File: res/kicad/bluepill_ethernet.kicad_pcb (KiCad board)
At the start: 2 copper layers, 50.4 x 50.4 mm, 47 parts, among them J1 HEADER-1x20, J2 Conn_01x03, J3 Conn_02x05_Odd_Even, J4 HEADER-1x20, J5 Conn_02x02_Odd_Even, J7 Conn_02x04_Odd_Even, SW1 SW_Push, U1 BluePill_STM32F103C, U2 93C46, U3 WIZ850io, U4 93C46, U5 PCF8574A, U6 LM75B

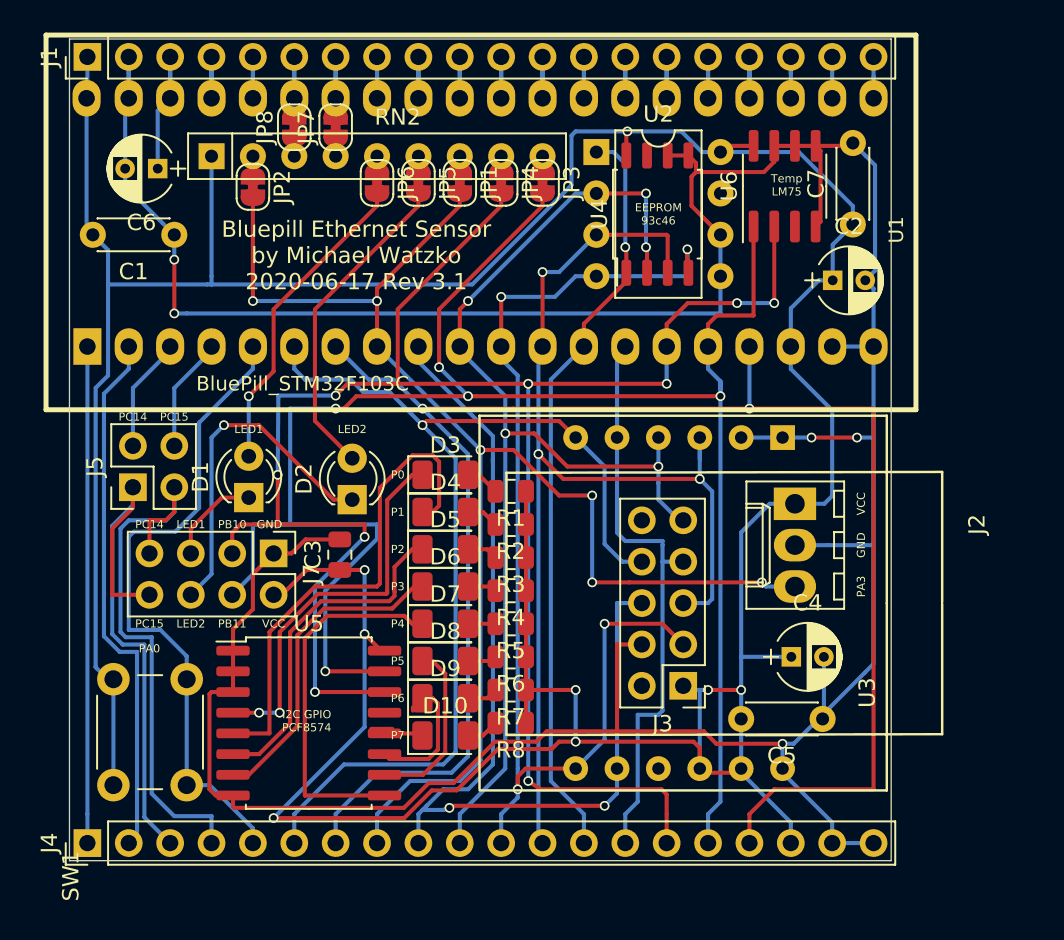
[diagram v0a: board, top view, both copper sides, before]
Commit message: Move molex pins and w5500 into 2,54mm raster
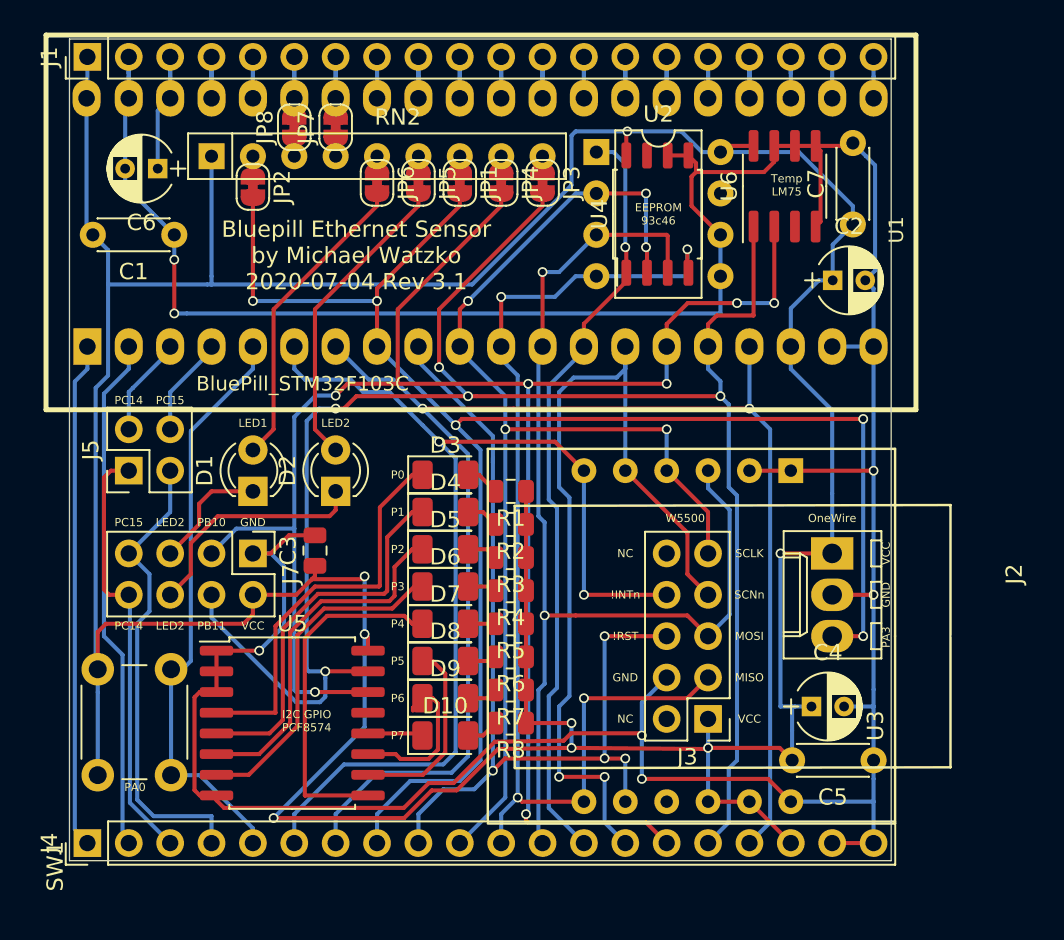
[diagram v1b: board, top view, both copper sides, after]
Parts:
- moved C5 4.03 mm to (92.2, 74.9)
- moved J2 3.81 mm to (89.7, 62.2)
- moved C4 3.29 mm to (88.4, 71.6)
- moved J3 2.54 mm to (82.0, 72.4)
- moved U3 2.09 mm to (87.1, 67.3)
- moved C3 1.55 mm to (57.9, 62.1)
- moved J7 1.27 mm to (54.1, 62.2)
- moved SW1 1.14 mm to (44.6, 75.8)
- moved D2 1.14 mm to (59.2, 58.4)
- moved J5 1.05 mm to (46.5, 57.1)
- moved U5 1.01 mm to (56.5, 72.6)
- moved D1 0.46 mm to (54.1, 58.4)
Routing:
- net Net-(J3-Pad7): track 36.1 -> 55.6 mm, vias 0 -> 2
- net Net-(J2-Pad3): track 88.9 -> 103.4 mm, vias 6 -> 5
- net Net-(J4-Pad17): track 105.7 -> 92.4 mm
- net VCC: track 248.8 -> 257.4 mm
- net Net-(J4-Pad3): track 34.0 -> 26.5 mm
- net Net-(D4-Pad1): track 30.8 -> 23.5 mm
- net i2c1c: track 123.7 -> 116.9 mm, vias 9 -> 7
- net Net-(D2-Pad1): track 21.0 -> 14.6 mm, vias 1 -> 0
- net Net-(J4-Pad4): track 34.4 -> 28.7 mm
- net Net-(J4-Pad5): track 40.2 -> 36.1 mm
- net Net-(J3-Pad6): track 61.3 -> 58.0 mm, vias 2 -> 4
- net i2c1d: track 118.2 -> 115.2 mm
- net Net-(J3-Pad9): track 70.3 -> 72.9 mm
- net Net-(J3-Pad8): track 64.8 -> 67.2 mm, vias 1 -> 2
- net Net-(J3-Pad5): track 69.9 -> 68.0 mm, vias 3 -> 2
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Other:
- board text added: "!INTn"
- board text added: "!RST"
- board text added: "Bluepill Ethernet Sensor by Michael Watzko 2020-07-04 Rev 3.1"
- board text added: "MISO"
- board text added: "MOSI"
- board text added: "NC"
- board text added: "OneWire"
- board text added: "SCLK"
- board text added: "SCNn"
- board text added: "W5500"
- board text removed: "Bluepill Ethernet Sensor by Michael Watzko 2020-06-17 Rev 3.1"

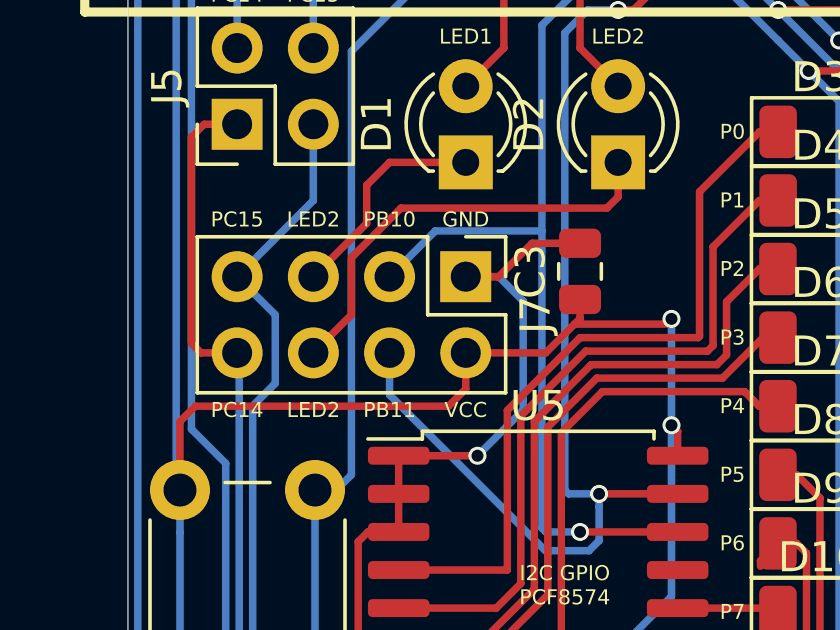
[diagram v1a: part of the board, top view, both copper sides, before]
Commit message: Add SCL and SDA labels to the pin header
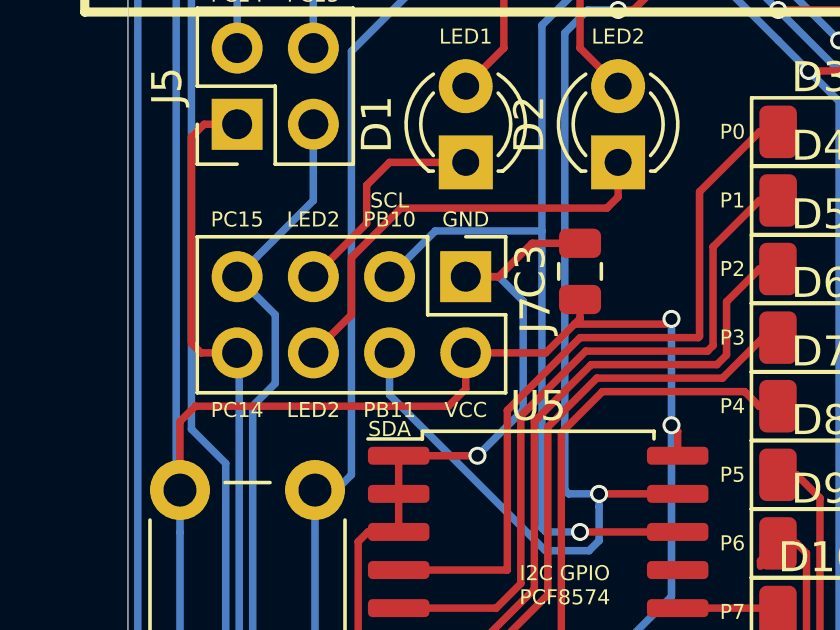
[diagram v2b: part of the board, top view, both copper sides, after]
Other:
- board text added: "SCL"
- board text added: "SDA"
